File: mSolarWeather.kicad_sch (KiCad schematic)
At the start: 18 parts, among them J1 WIND, J2 RAIN, J3 JST2PH Batt LiFePo4, J4 BME280_I2C, J5 USB C, J6 Conn_01x04, SW1 SW_Push_Dual, SW2 SW_Push_Dual, U1 ESP32-S3-WROOM-1, U2 XC6220B331MR, U3 BQ297xy

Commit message: Update mSolarWeather.kicad_sch
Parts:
- added J8: Solar connector, TerminalBlock_Phoenix:TerminalBlock_Phoenix_MKDS-1,5-2-5.08_1x02_P5.08mm_Horizontal, symbol Connector_Generic:Conn_01x02
- U1: value ESP32-S3-WROOM-1 -> ESP32-S3-WROOM-1-N16R2; Mouser (none) -> https://www.mouser.fr/ProductDetail/356-ESP32S3WRM1N16R2
- U3: value BQ297xy -> BQ29706
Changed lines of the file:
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@@
 			)
 		)
-		(property "Value" "ESP32-S3-WROOM-1"
+		(property "Value" "ESP32-S3-WROOM-1-N16R2"
 			(at 143.1641 82.55 0)
 			(effects
@@
 		)
 		(property "Description" "RF Module, ESP32-S3 SoC, Wi-Fi 802.11b/g/n, Bluetooth, BLE, 32-bit, 3.3V, onboard antenna, SMD"
+			(at 140.97 110.49 0)
+			(effects
+				(font
+					(size 1.27 1.27)
+				)
+				(hide yes)
+			)
+		)
+		(property "Mouser" "https://www.mouser.fr/ProductDetail/356-ESP32S3WRM1N16R2"
 			(at 140.97 110.49 0)
 			(effects
@@
 			)
 		)
-		(property "Value" "BQ297xy"
+		(property "Value" "BQ29706"
 			(at 46.99 78.74 0)
 			(effects
@@
 					(unit 1)
 				)
+			)
+		)
+	)
+	(symbol
+		(lib_id "Connector_Generic:Conn_01x02")
+		(at 58.42 22.86 180)
+		(unit 1)
+		(exclude_from_sim no)
+		(in_bom yes)
+		(on_board yes)
+		(dnp no)
+		(fields_autoplaced yes)
+		(property "Reference" "J8"
+			(at 58.42 13.97 0)
+			(effects
+				(font
+					(size 1.27 1.27)
+				)
+			)
+		)
+		(property "Value" "Solar connector"
+			(at 58.42 16.51 0)
+			(effects
+				(font
+					(size 1.27 1.27)
+				)
+			)
+		)
+		(property "Footprint" "TerminalBlock_Phoenix:TerminalBlock_Phoenix_MKDS-1,5-2-5.08_1x02_P5.08mm_Horizontal"
+			(at 58.42 22.86 0)
+			(effects
+				(font
+					(size 1.27 1.27)
+				)
+				(hide yes)
+			)
+		)
+		(property "Datasheet" "~"
+			(at 58.42 22.86 0)
+			(effects
+				(font
+					(size 1.27 1.27)
+				)
+				(hide yes)
+			)
+		)
+		(property "Description" "Generic connector, single row, 01x02, script generated (kicad-library-utils/schlib/autogen/connector/)"
+			(at 58.42 22.86 0)
+			(effects
+				(font
+					(size 1.27 1.27)
+				)
+				(hide yes)
+			)
+		)
+		(pin "1"
+		)
+		(pin "2"
+		)
+		(instances
+			(project ""
+				(path "/8cb2730a-92d4-4d73-8ee8-3d09d9726f54"
+					(reference "J8")
+					(unit 1)
+				)

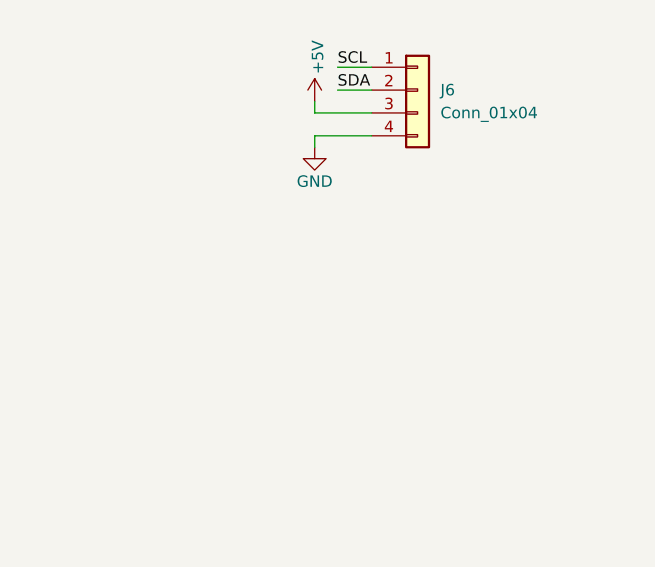
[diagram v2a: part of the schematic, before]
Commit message: Add Stemma QT connector
JST_SH_SM04B like ?
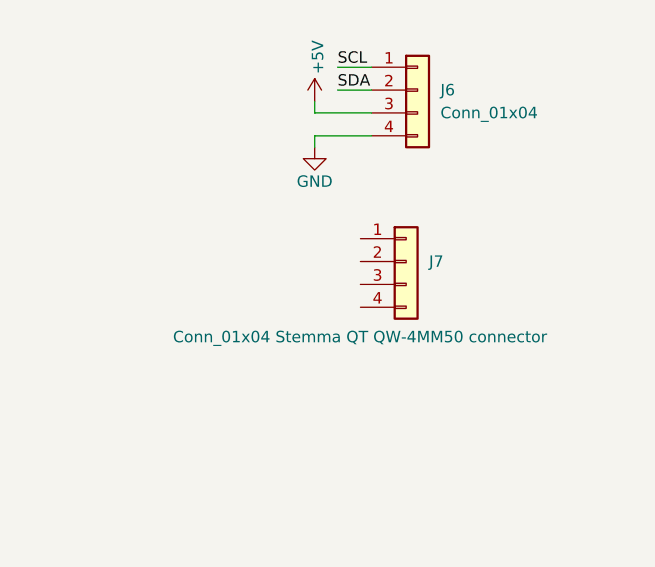
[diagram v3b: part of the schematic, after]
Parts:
- added J7: Conn_01x04 Stemma QT QW-4MM50 connector, Connector_JST:JST_SH_SM04B-SRSS-TB_1x04-1MP_P1.00mm_Horizontal, symbol Connector_Generic:Conn_01x04
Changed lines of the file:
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@@
+	)
+	(symbol
+		(lib_id "Connector_Generic:Conn_01x04")
+		(at 264.16 118.11 0)
+		(unit 1)
+		(exclude_from_sim no)
+		(in_bom yes)
+		(on_board yes)
+		(dnp no)
+		(property "Reference" "J7"
+			(at 266.7 118.1099 0)
+			(effects
+				(font
+					(size 1.27 1.27)
+				)
+				(justify left)
+			)
+		)
+		(property "Value" "Conn_01x04  Stemma QT QW-4MM50 connector"
+			(at 238.252 126.492 0)
+			(effects
+				(font
+					(size 1.27 1.27)
+				)
+				(justify left)
+			)
+		)
+		(property "Footprint" "Connector_JST:JST_SH_SM04B-SRSS-TB_1x04-1MP_P1.00mm_Horizontal"
+			(at 264.16 118.11 0)
+			(effects
+				(font
+					(size 1.27 1.27)
+				)
+				(hide yes)
+			)
+		)
+		(property "Datasheet" "~"
+			(at 264.16 118.11 0)
+			(effects
+				(font
+					(size 1.27 1.27)
+				)
+				(hide yes)
+			)
+		)
+		(property "Description" "Generic connector, single row, 01x04, script generated (kicad-library-utils/schlib/autogen/connector/)"
+			(at 264.16 118.11 0)
+			(effects
+				(font
+					(size 1.27 1.27)
+				)
+				(hide yes)
+			)
+		)
+		(pin "3"
+		)
+		(pin "1"
+		)
+		(pin "2"
+		)
+		(pin "4"
+		)
+		(instances
+			(project "mSolarWeather"
+				(path "/8cb2730a-92d4-4d73-8ee8-3d09d9726f54"
+					(reference "J7")
+					(unit 1)
+				)
+			)
+		)
 	)
 	(symbol

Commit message: Update mSolarWeather.kicad_sch
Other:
- note added: "TPS63020 Buck-boost Converter (TODO) MAX17048 batt manager (TODO) bq25185 USB / DC / Solar Lithium Ion/Polymer charger (TODO)"
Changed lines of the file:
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@@
 		(comment 1 "For safety this design is for Batt LiFePo4")
+	)
+	(text "TPS63020 Buck-boost Converter (TODO) \nMAX17048 batt manager (TODO)\nbq25185 USB / DC / Solar Lithium Ion/Polymer charger (TODO)"
+		(exclude_from_sim no)
+		(at 178.054 160.02 0)
+		(effects
+			(font
+				(size 1.27 1.27)
+			)
+			(justify left)
+		)
 	)
 	(junction

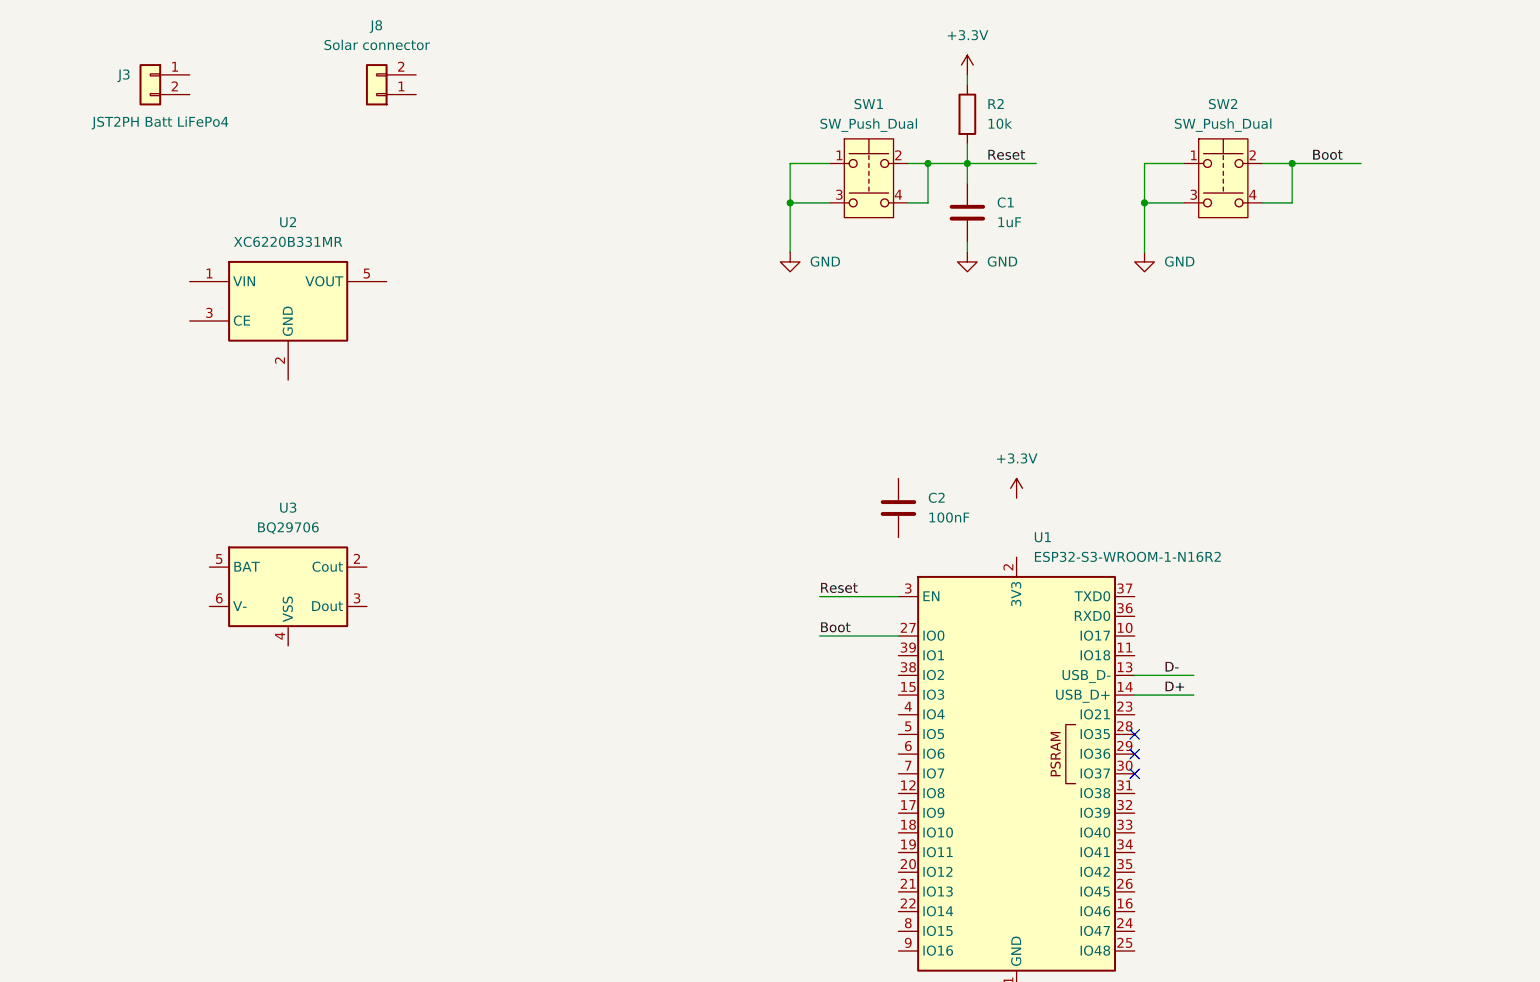
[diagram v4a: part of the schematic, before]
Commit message: Update schematic with the TPS63021
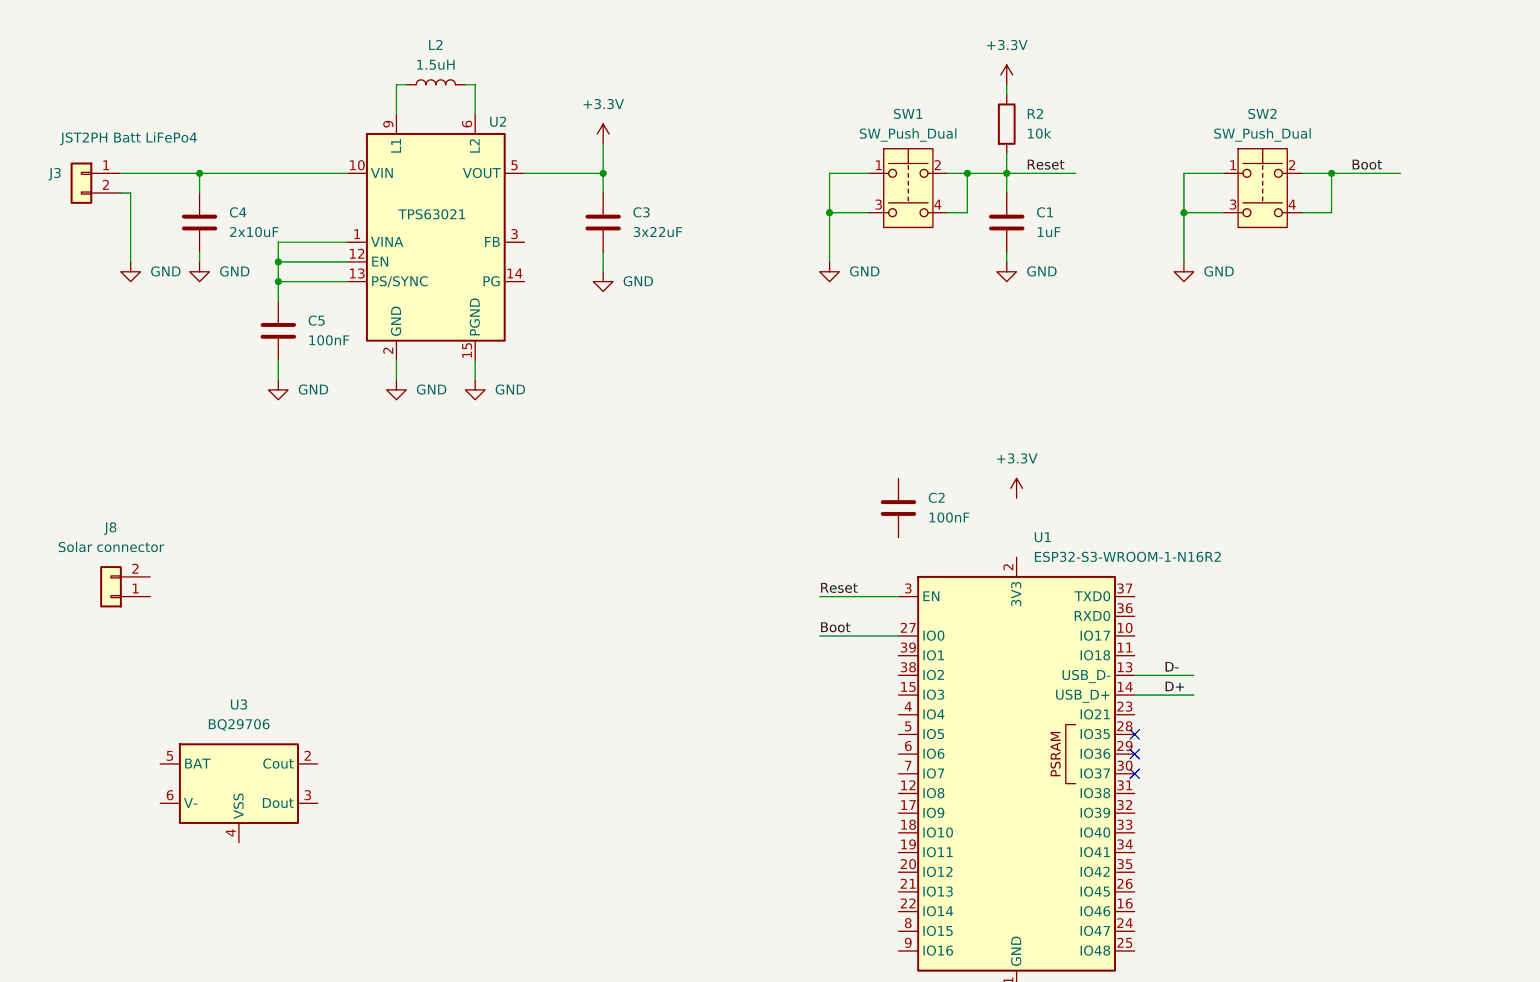
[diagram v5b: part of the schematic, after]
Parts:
- removed U2: XC6220B331MR, Package_TO_SOT_SMD:SOT-23-5, symbol Regulator_Linear:XC6220B331MR
- added C3: 3x22uF, symbol Device:C
- added C4: 2x10uF, symbol Device:C
- added C5: 100nF, symbol Device:C
- added L2: 1.5uH, Inductor_SMD_Wurth:L_Wurth_WE-LQSH-2010, symbol Device:L
- added U2: TPS63021, mSolarLib:VSON_DSJ-14-3x4mm_P0.5mm_ThermalVias, symbol mSolarLib:TPS63021
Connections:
- net +3.3V: now also C3.1, U2.4 (VOUT), U2.5 (VOUT)
- net GND: now also J3.2 (Pin_2), C3.2, C4.2, C5.2, U2.15 (PGND), U2.2 (GND)
- net at J3.1 (Pin_1): now also C4.1, U2.10 (VIN), U2.11 (VIN)
- new net: C5.1, U2.1 (VINA), U2.12 (EN), U2.13 (PS/SYNC)
- new net: L2.2, U2.6 (L2), U2.7 (L2)
- new net: L2.1, U2.8 (L1), U2.9 (L1)
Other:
- moved on the sheet: C1, J3, J8, R2, SW1, SW2, U3

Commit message: Update mSolarWeather.kicad_sch
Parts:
- added C2: 10uF, symbol Device:C
- added C5, C6: 22uF, symbol Device:C
- C1: renamed from C4; value 2x10uF -> 10uF
- C3: renamed from C5; footprint (none) -> Capacitor_SMD:C_0805_2012Metric_Pad1.18x1.45mm_HandSolder
- C4: renamed from C3; value 3x22uF -> 22uF
- C7: renamed from C1; footprint (none) -> Capacitor_SMD:C_0805_2012Metric_Pad1.18x1.45mm_HandSolder
- C8: renamed from C2; footprint (none) -> Capacitor_SMD:C_0805_2012Metric_Pad1.18x1.45mm_HandSolder
- R1: renamed from R3; footprint (none) -> Resistor_SMD:R_0805_2012Metric_Pad1.20x1.40mm_HandSolder
- R2: renamed from R1; footprint (none) -> Resistor_SMD:R_0805_2012Metric_Pad1.20x1.40mm_HandSolder
- R3: renamed from R5; footprint (none) -> Resistor_SMD:R_0805_2012Metric_Pad1.20x1.40mm_HandSolder
- R4: renamed from R2; footprint (none) -> Resistor_SMD:R_0805_2012Metric_Pad1.20x1.40mm_HandSolder
- renumbered D3 to D1, J3 to J1, J8 to J2, J5 to J3, J6 to J5, J7 to J6, J1 to J7, J2 to J8, L2 to L1, U3 to U1, U1 to U3
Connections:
- net +3.3V: now also C5.1, C6.1
- net GND: now also C2.2, C5.2, C6.2
- net at C1.1, J1.1 (Pin_1), U2.10 (VIN)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: now also C2.1
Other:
- company: cf -> cfdev
- moved on the sheet: C3, C4, C7, C8, D1, J3, J4, J5, J6, J7, J8, L1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
